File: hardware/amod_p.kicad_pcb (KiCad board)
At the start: 2 copper layers, 100 x 100 mm, 150 parts, among them J1001 SMA, J1002 SMA, J101 SMA, J102 SMA, J1101 SMA, J1102 SMA, J1103 SMA, J1104 SMA, J1105 SMA, J1201 SMA, J1301 SMA, J1302 coil, J201 SMA, J202 SMA, J301 SMA, J302 SMA, J401 SMA, J402 SMA, J501 SMA, J502 SMA, J601 SMA, J602 SMA, J701 SMA, J702 SMA, J801 SMA, J802 SMA, J901 SMA, J902 SMA, SW1201 DIP4, SW1301 DIP4, SW401 DIP2, Y801 4 MHz, Y901 455 kHz

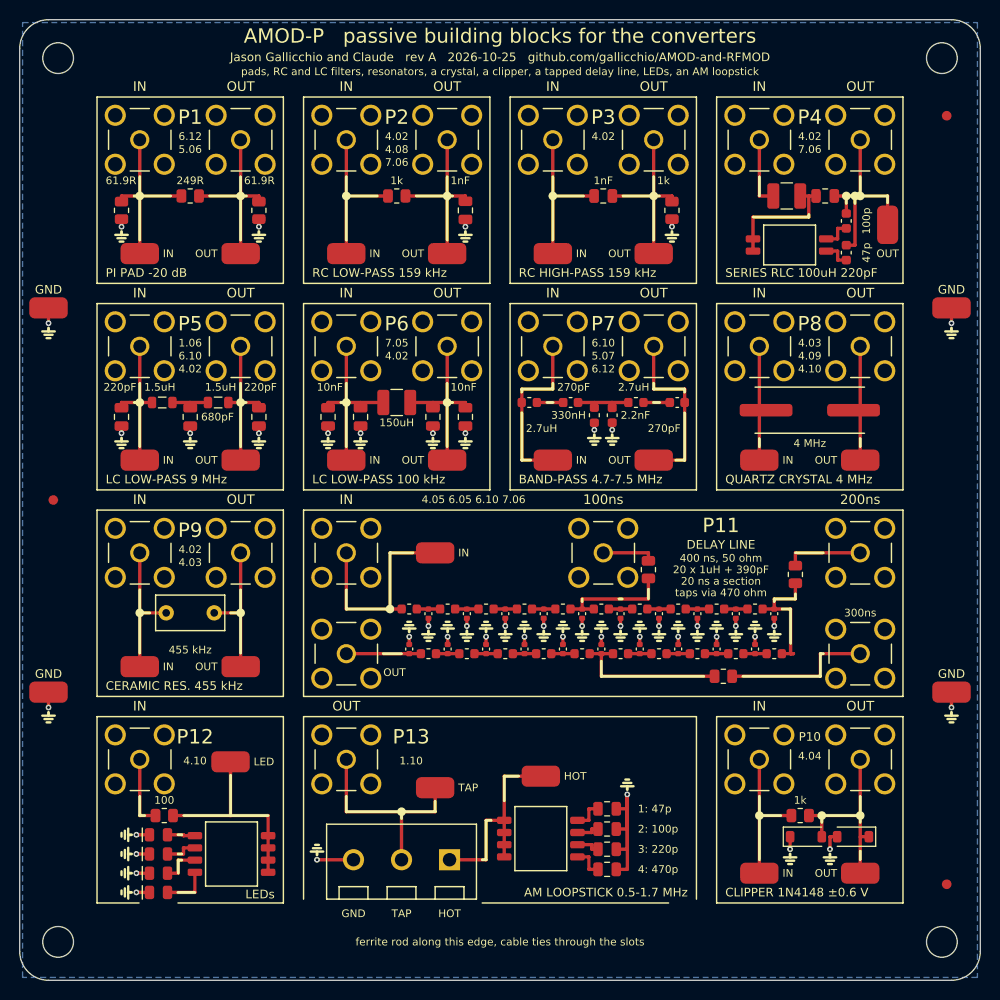
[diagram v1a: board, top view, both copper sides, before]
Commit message: Jacks in a checkerboard on every board (Prompt 12): every pair 14.85 mm or more
IN at a cell's top-left slot, OUT at its bottom-right, a two-cell tile's third jack
at its right cell's top-left.  geometry.py now asserts 14.3 mm between every pair.

- AMOD-P: all thirteen tiles re-laid; P8's crystal and P9's resonator at 45 degrees
  (P8's jacks 0.5 mm further out, slots TLo/BRo); P11's taps on TL/BR slots.
- AMOD-A: A2-A4 share opa_tile_br; A4's OPA847 now SOT-23-6 (C160422); A7 now
  Nexperia's 74HC4046APW-Q100J in TSSOP-16 (C546981, 234 in stock); A8, A9 and A11
  re-laid with OUT at the bottom-right; the back's QR code moved.  $50.90 of parts.
- RF-MOD: the mixers' LO jacks moved from the top middle to TL1.
- Assembler's notes say the 45-degree parts are meant; PLAN, DOA, review brief,
  README and the chat log updated.

All three boards: ERC 0, DRC 0, every fab check passed.

Co-Authored-By: Claude Opus 5.5 <noreply@anthropic.com>
Claude-Session: https://claude.ai/code/session_01RKeoKvFFzjk3cEBLCXXHnB
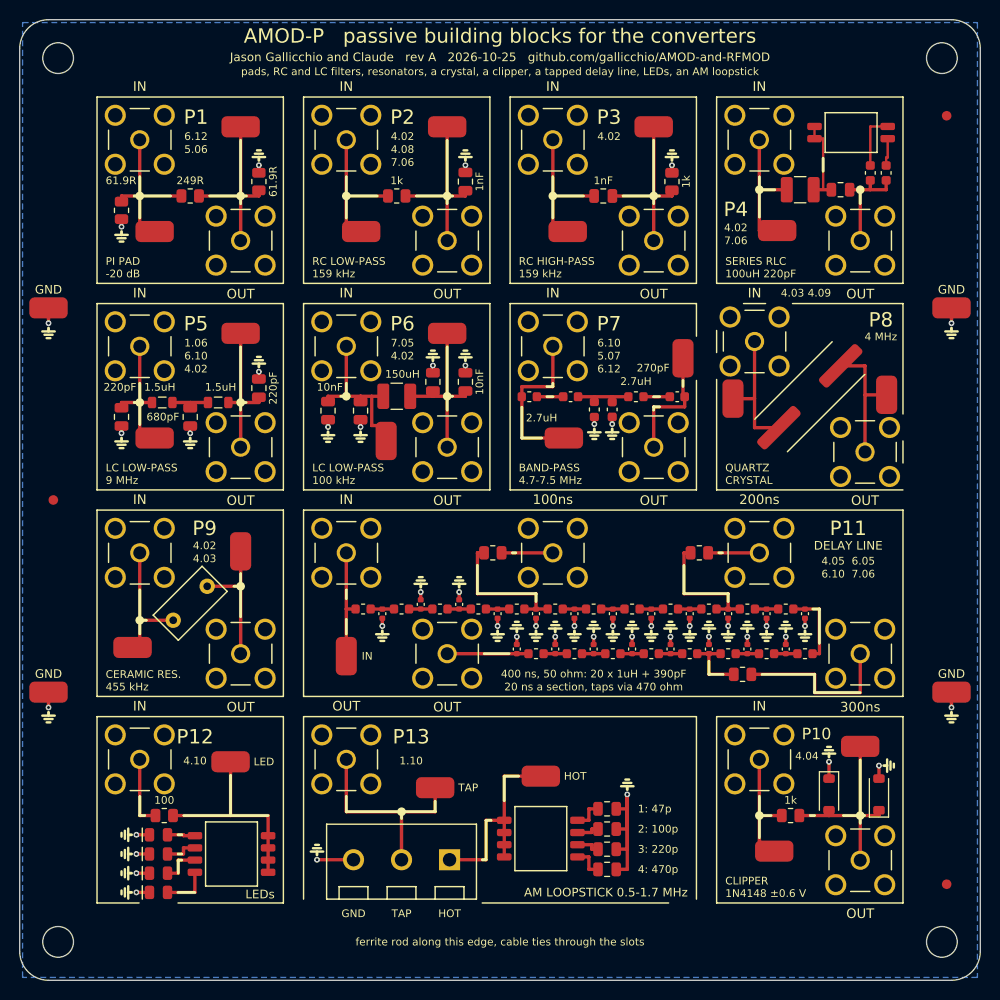
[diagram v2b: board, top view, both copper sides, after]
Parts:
- TP401: value OUT -> IN
- moved R1101 16.3 mm to (49.2, 55.5), turned to 0 degrees
- moved TP1101 14.2 mm to (34.0, 66.2), turned to 90 degrees
- moved SW401 13.3 mm to (86.5, 11.8)
- moved TP502 13.2 mm to (23.0, 32.6)
- moved TP602 13.2 mm to (44.5, 32.6)
- moved TP102 13.2 mm to (23.0, 11.2)
- moved TP202 13.2 mm to (44.5, 11.2)
- moved TP302 13.2 mm to (66.0, 11.2)
- moved TP1002 13.2 mm to (87.5, 75.7)
- moved TP902 12.0 mm to (23.0, 55.4), turned to 90 degrees
- moved TP401 11.5 mm to (78.8, 21.9), turned to 0 degrees
- moved C1113 11.2 mm to (79.8, 65.5)
- moved C1114 11.2 mm to (75.8, 65.5)
- moved C1115 11.2 mm to (71.8, 65.5)
- moved C1116 11.2 mm to (67.8, 65.5)
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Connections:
- C402 pad 1: /P4_OUT -> Net-(C402-Pad1)
- C402 pad 2: Net-(C402-Pad2) -> /P4_OUT
- C403 pad 1: /P4_OUT -> Net-(C403-Pad1)
- C403 pad 2: Net-(C403-Pad2) -> /P4_OUT
- R1101 pad 1: Net-(J1102-In) -> /P11_T1
- R1101 pad 2: /P11_T1 -> Net-(J1102-In)
- R1102 pad 1: Net-(J1103-In) -> /P11_T2
- R1102 pad 2: /P11_T2 -> Net-(J1103-In)
- SW401 pad 1: Net-(C403-Pad2) -> Net-(C403-Pad1)
- SW401 pad 2: Net-(C402-Pad2) -> Net-(C402-Pad1)
- TP401 pad 1: /P4_OUT -> /P4_IN
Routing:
- net /P4_OUT: track 22.3 -> 11.0 mm
- net Net-(J1101-In): track 22.2 -> 11.7 mm
- net /P11_T3: track 16.6 -> 7.16 mm
- net /P4_IN: track 7.30 -> 14.1 mm
- net Net-(C402-Pad1): track 0.00 -> 5.87 mm
- net /P7_OUT: track 18.3 -> 12.5 mm
- net Net-(C1112-Pad1): track 2.43 -> 8.08 mm
- net /P4_N1: track 13.2 -> 9.33 mm
- net Net-(C402-Pad2): track 3.18 -> 0.00 mm
- net Net-(C403-Pad2): track 3.03 -> 0.00 mm
- net Net-(C403-Pad1): track 0.00 -> 2.95 mm
- net Net-(J1103-In): track 8.09 -> 5.34 mm
- net /P11_T1: track 12.5 -> 15.1 mm
- net /P8_OUT: track 11.9 -> 13.8 mm
- net /P8_IN: track 11.9 -> 13.8 mm
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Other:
- board text added: "-20 dB"
- board text added: "100 kHz"
- board text added: "100uH 220pF"
- board text added: "159 kHz"
- board text added: "1N4148 ±0.6 V"
- board text added: "20 ns a section, taps via 470 ohm"
- board text added: "4 MHz"
- board text added: "4.03 4.09"
- board text added: "4.05 6.05"
- board text added: "4.7-7.5 MHz"
- board text added: "400 ns, 50 ohm: 20 x 1uH + 390pF"
- board text added: "455 kHz"
- board text added: "6.10 7.06"
- board text added: "9 MHz"
- board text added: "BAND-PASS"
- board text added: "CERAMIC RES."
- board text added: "CLIPPER"
- board text added: "CRYSTAL"
- board text added: "LC LOW-PASS"
- board text added: "PI PAD"
- board text added: "QUARTZ"
- board text added: "RC HIGH-PASS"
- board text added: "RC LOW-PASS"
- board text added: "SERIES RLC"
- board text removed: "20 ns a section"
- board text removed: "20 x 1uH + 390pF"
- board text removed: "4.05 6.05 6.10 7.06"
- board text removed: "4.09"
- board text removed: "400 ns, 50 ohm"
- board text removed: "BAND-PASS 4.7-7.5 MHz"
- board text removed: "CERAMIC RES. 455 kHz"
- board text removed: "CLIPPER 1N4148 ±0.6 V"
- board text removed: "LC LOW-PASS 100 kHz"
- board text removed: "LC LOW-PASS 9 MHz"
- board text removed: "PI PAD -20 dB"
- board text removed: "QUARTZ CRYSTAL 4 MHz"
- board text removed: "RC HIGH-PASS 159 kHz"
- board text removed: "RC LOW-PASS 159 kHz"
- board text removed: "SERIES RLC 100uH 220pF"
- board text removed: "taps via 470 ohm"

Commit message: Silkscreen says what each tile is and whose jack is whose: jack names on their own tile's frame, titles in words on the top frame, ranges and levels placed inside; tutorial section numbers off the boards; README tables of every tile (what, chip link, specs, limits, experiments, use, what to buy) and handbook entries as tables with a picture of each tile, both from boards/tile_docs.py
Co-Authored-By: Claude Opus 5.5 <noreply@anthropic.com>
Claude-Session: https://claude.ai/code/session_01RKeoKvFFzjk3cEBLCXXHnB
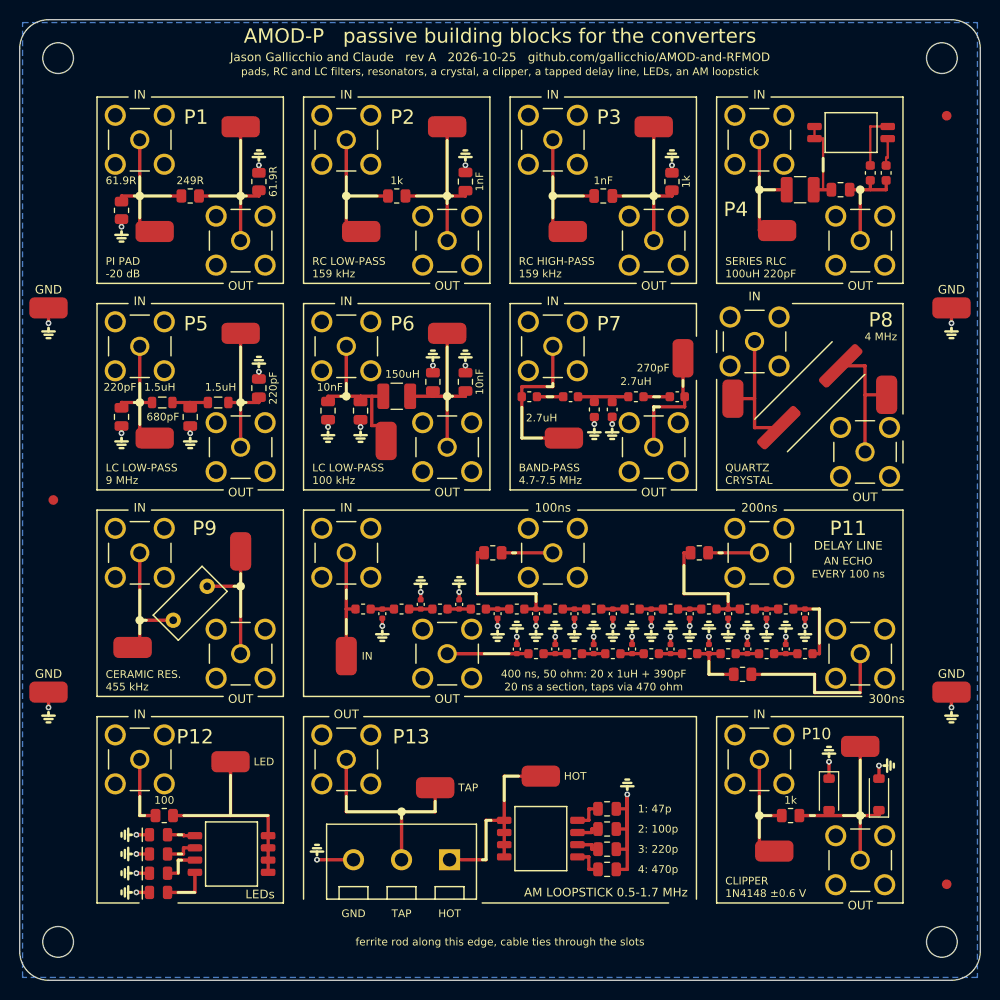
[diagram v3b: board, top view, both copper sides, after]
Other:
- board text added: "AN ECHO"
- board text added: "EVERY 100 ns"
- board text removed: "1.06"
- board text removed: "1.10"
- board text removed: "4.02"
- board text removed: "4.03"
- board text removed: "4.03 4.09"
- board text removed: "4.04"
- board text removed: "4.05 6.05"
- board text removed: "4.08"
- board text removed: "4.10"
- board text removed: "5.06"
- board text removed: "5.07"
- board text removed: "6.10"
- board text removed: "6.10 7.06"
- board text removed: "6.12"
- board text removed: "7.05"
- board text removed: "7.06"

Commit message: P13: a VAR C screw terminal beside the coil's for an external tuning capacitor (a polyvaricon and its dial do not fit a cell); the DIP and its capacitors moved up into the right cell's top half; KIT.md lists a 365 pF air variable
Co-Authored-By: Claude Opus 5.5 <noreply@anthropic.com>
Claude-Session: https://claude.ai/code/session_01RKeoKvFFzjk3cEBLCXXHnB
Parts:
- added J1303: VAR C, amod:TerminalBlock_KF301_1x02_P5.00mm, F.Cu at (57.2, 87.5)
- moved TP1302 13.4 mm to (66.2, 84.7)
- moved C1301 8.36 mm to (62.1, 73.8)
- moved C1302 8.26 mm to (62.1, 76.0)
- moved C1303 8.13 mm to (62.1, 78.3)
- moved C1304 8.06 mm to (62.1, 80.5)
- moved SW1301 7.60 mm to (54.2, 77.7)
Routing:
- net /P13_HOT: track 22.0 -> 44.9 mm
- net GND: track 67.9 -> 70.7 mm, vias 45 -> 46
- net Net-(C1301-Pad1): track 3.33 -> 5.04 mm
- net Net-(C1302-Pad1): track 2.50 -> 4.11 mm
- net Net-(C1304-Pad1): track 3.44 -> 4.03 mm
- net Net-(C1303-Pad1): track 2.60 -> 3.14 mm
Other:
- board text added: "0.5-1.7 MHz"
- board text added: "AM LOOPSTICK"
- board text added: "OPTIONAL"
- board text added: "VAR C"
- board text added: "expected response. P13: a 330 uH ferrite-rod coil along this edge, under cable ties; a tuning capacitor on VAR C."
- board text removed: "AM LOOPSTICK 0.5-1.7 MHz"
- board text removed: "expected response. P13 wants a ferrite-rod coil (about 330 uH) along this edge, under cable ties through the slots."

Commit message: Silk case convention on all six boards (Jason, Prompt 17: "To distinguish whole-tile labels from SMA or port labels, use different cases")
Ports (the jacks' names, terminal and loop names, a port named inside a note) stay UPPER CASE.  A tile's label (its
title on the frame, its name in the corner) is Mixed case: the first letter capitalised and the rest as written ("RC
low-pass", "Synthesizer", "I/Q demodulator"; tiles.label_case).  Ranges, values and notes are lower case except units,
acronyms and part numbers ("loss 1.7 dB", "OUT floats").  RF-MOD-2's X1 and X2 take word titles with their chips in
the info; RF-MOD's and RF-MOD-2's LNA tiles are titled "Preamp" ("Low-noise amp" does not fit a cell's frame); a few
two-line labels moved 0.15-0.3 mm for the descenders mixed case brings.  AMOD-P2's tile records (tile_docs), its DOA
list, KIT.md's AMOD-P2 section; X5's calibration points at P14.  All six boards: ERC 0, DRC 0, all fab checks.

Co-Authored-By: Claude Opus 5.5 <noreply@anthropic.com>
Claude-Session: https://claude.ai/code/session_01RKeoKvFFzjk3cEBLCXXHnB
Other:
- board text added: "AM loopstick"
- board text added: "Band-pass"
- board text added: "Ceramic res."
- board text added: "Clipper"
- board text added: "Delay line"
- board text added: "LC low-pass"
- board text added: "Pi pad"
- board text added: "Quartz"
- board text added: "RC high-pass"
- board text added: "RC low-pass"
- board text added: "Series RLC"
- board text added: "an echo"
- board text added: "crystal"
- board text added: "every 100 ns"
- board text added: "optional"
- board text removed: "AM LOOPSTICK"
- board text removed: "AN ECHO"
- board text removed: "BAND-PASS"
- board text removed: "CERAMIC RES."
- board text removed: "CLIPPER"
- board text removed: "CRYSTAL"
- board text removed: "DELAY LINE"
- board text removed: "EVERY 100 ns"
- board text removed: "LC LOW-PASS"
- board text removed: "OPTIONAL"
- board text removed: "PI PAD"
- board text removed: "QUARTZ"
- board text removed: "RC HIGH-PASS"
- board text removed: "RC LOW-PASS"
- board text removed: "SERIES RLC"
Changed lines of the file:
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@@
 	(gr_line
 		(start 35.815714 72.55)
-		(end 49.618572 72.55)
+		(end 50.81857 72.55)
 		(stroke
 			(width 0.15)
@@
 		(layer "Edge.Cuts")
 	)
-	(gr_text "PI PAD"
-		(at 8.95 25.15 0)
+	(gr_text "Pi pad"
+		(at 8.95 24.95 0)
 		(layer "F.SilkS")
 		(effects
@@
 		)
 	)
-	(gr_text "LC LOW-PASS"
-		(at 8.95 46.65 0)
+	(gr_text "LC low-pass"
+		(at 8.95 46.45 0)
 		(layer "F.SilkS")
 		(effects
@@
 		)
 	)
-	(gr_text "CERAMIC RES."
-		(at 8.95 68.15 0)
+	(gr_text "Ceramic res."
+		(at 8.95 67.95 0)
 		(layer "F.SilkS")
 		(effects
@@
 		)
 	)
-	(gr_text "RC LOW-PASS"
-		(at 30.45 25.15 0)
+	(gr_text "RC low-pass"
+		(at 30.45 24.95 0)
 		(layer "F.SilkS")
 		(effects
@@
 		)
 	)
-	(gr_text "LC LOW-PASS"
-		(at 30.45 46.65 0)
+	(gr_text "LC low-pass"
+		(at 30.45 46.45 0)
 		(layer "F.SilkS")
 		(effects
@@
 		)
 	)
-	(gr_text "RC HIGH-PASS"
-		(at 51.95 25.15 0)
+	(gr_text "RC high-pass"
+		(at 51.95 24.95 0)
 		(layer "F.SilkS")
 		(effects
@@
 		)
 	)
-	(gr_text "BAND-PASS"
-		(at 51.95 46.65 0)
+	(gr_text "Band-pass"
+		(at 51.95 46.45 0)
 		(layer "F.SilkS")
 		(effects
@@
 	)
 	(gr_text "VAR C"
-		(at 64.05 88.45 0)
+		(at 64.25 88.45 0)
 		(layer "F.SilkS")
 		(effects
@@
 		)
 	)
-	(gr_text "OPTIONAL"
-		(at 64.05 89.85 0)
+	(gr_text "optional"
+		(at 64.25 89.85 0)
 		(layer "F.SilkS")
 		(effects
@@
 		)
 	)
-	(gr_text "SERIES RLC"
-		(at 73.45 25.15 0)
+	(gr_text "Series RLC"
+		(at 73.45 24.95 0)
 		(layer "F.SilkS")
 		(effects
@@
 		)
 	)
-	(gr_text "QUARTZ"
-		(at 73.45 46.65 0)
+	(gr_text "Quartz"
+		(at 73.45 46.45 0)
 		(layer "F.SilkS")
 		(effects
@@
 		)
 	)
-	(gr_text "CRYSTAL"
+	(gr_text "crystal"
 		(at 73.45 47.95 0)
 		(layer "F.SilkS")
@@
 		)
 	)
-	(gr_text "CLIPPER"
-		(at 73.45 89.65 0)
+	(gr_text "Clipper"
+		(at 73.45 89.45 0)
 		(layer "F.SilkS")
 		(effects
@@
 		)
 	)
-	(gr_text "AN ECHO"
+	(gr_text "an echo"
 		(at 86.25 56.35 0)
 		(layer "F.SilkS")
@@
 		)
 	)
-	(gr_text "EVERY 100 ns"
+	(gr_text "every 100 ns"
 		(at 86.25 57.7 0)
 		(layer "F.SilkS")
@@
 		)
 	)
-	(gr_text "DELAY LINE"
+	(gr_text "Delay line"
 		(at 86.25 54.75 0)
 		(layer "F.SilkS")
@@
 		)
 	)
-	(gr_text "AM LOOPSTICK"
-		(at 49.968572 72.55 0)
+	(gr_text "AM loopstick"
+		(at 51.16857 72.55 0)
 		(layer "F.SilkS")
 		(effects

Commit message: Back-side panels on all six boards; P22 set by hand or by the FPGA; P15 dropped
Jason, Prompt 18: "I hope that the silkscreen (including on the back) is appropriately used to document anything that a
user definitely needs to know to use the tiles successfully and without damaging anything.  If there is additional room
on the back, putting plots of expected responses or other relevant parameters would be great."

- gen_pcb.back_panels: under each tile, mirrored on the back silk, its number and title and the lines in its board's
  BACK dict (levels, loads, supplies, cautions), and where there is one its expected response as a small plot
  (BACK_PLOTS, or the ladder tiles' own simulation; scripts/backplots.py for the rest: amplifiers, datasheet tables,
  the open stub, P23's tuning curve, P10's clipping curve).  A panel goes as one block or in two to four parts, each
  below the one before, clear of the back's tracks and vias where it can be; every panel and plot placed, DRC 0.
- Front silk: Y2 says PULSES ONLY, Y10 "start at mV", R5 and X4 their input level (IN -20 dBm) in place of the noise
  figure.
- P22 (PE43711) on two cells with an 8-way DIP switch: way 1 SPI, ways 2-8 the bits (direct parallel mode with LE pulled
  high), 100 k pull-downs; it still needs the Pmod's 3.3 V.  P15 (two Smith-chart loads) dropped for the cell; P23 moved
  to (3,0).

Co-Authored-By: Claude Opus 5.5 <noreply@anthropic.com>
Claude-Session: https://claude.ai/code/session_01RKeoKvFFzjk3cEBLCXXHnB
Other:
- board text added: "+4V"
- board text added: "-14 dB if high-Z"
- board text added: "-20 dB, 50 ohm"
- board text added: "-30 dB 18 MHz"
- board text added: "0 to -30 dB"
- board text added: "0 to -50 dB"
- board text added: "0 to -60 dB"
- board text added: "0.4-1.3 MHz"
- board text added: "1.07-0.83 MHz"
- board text added: "100M"
- board text added: "100k"
- board text added: "10M"
- board text added: "10k"
- board text added: "1: +47 pF"
- board text added: "1: 630 nm"
- board text added: "1M"
- board text added: "1k"
- board text added: "20 ns a section"
- board text added: "2: +100 pF"
- board text added: "2: 596 nm"
- board text added: "30M"
- board text added: "330 uH coil"
- board text added: "3: 525 nm"
- board text added: "455 kHz series"
- board text added: "4: 469 nm"
- board text added: "50 ohm both"
- board text added: "50 ohm both ends"
- board text added: "ADC on high-Z"
- board text added: "IN -4V"
- board text added: "IN 0-5 V"
- board text added: "IN max +-3 V"
- board text added: "IN max +-4 V"
- board text added: "OUT +-1 V"
- board text added: "OUT: 1 k source"
- board text added: "OUT: high-Z"
- board text added: "P1 Pi pad"
- board text added: "P10 Clipper"
- board text added: "P11 Delay line"
- board text added: "P12 LEDs"
- board text added: "P13 AM loopstick"
- board text added: "P2 RC low-pass"
- board text added: "P3 RC high-pass"
- board text added: "P4 Series RLC"
- board text added: "P5 LC low-pass"
- board text added: "P6 LC low-pass"
- board text added: "P7 Band-pass"
- board text added: "P8 Quartz crystal"
- board text added: "P9 Ceramic res."
- board text added: "Q a few 100"
- board text added: "Q about 50,000"
- board text added: "Q about 6"
- board text added: "VAR C: outside"
- board text added: "cut-off 16 MHz"
- board text added: "drive < +-1 V"
- board text added: "ends"
- board text added: "flat passband"
- board text added: "fs 4.000 MHz"
- board text added: "one peak, no"
- board text added: "step a few Hz"
- board text added: "taps /10 50 ohm"
- board text added: "taps x1 high-Z"
- board text added: "tau 1 us"
- board text added: "then A4's LNA"
- board text added: "tuning cap"
